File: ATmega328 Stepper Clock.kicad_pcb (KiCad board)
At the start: 2 copper layers, 80 x 80 mm, 9 parts, among them IC1 ATMEGA328-AU, J2 SBH11-PBPC-D05-ST-BK, Y1 Crystal

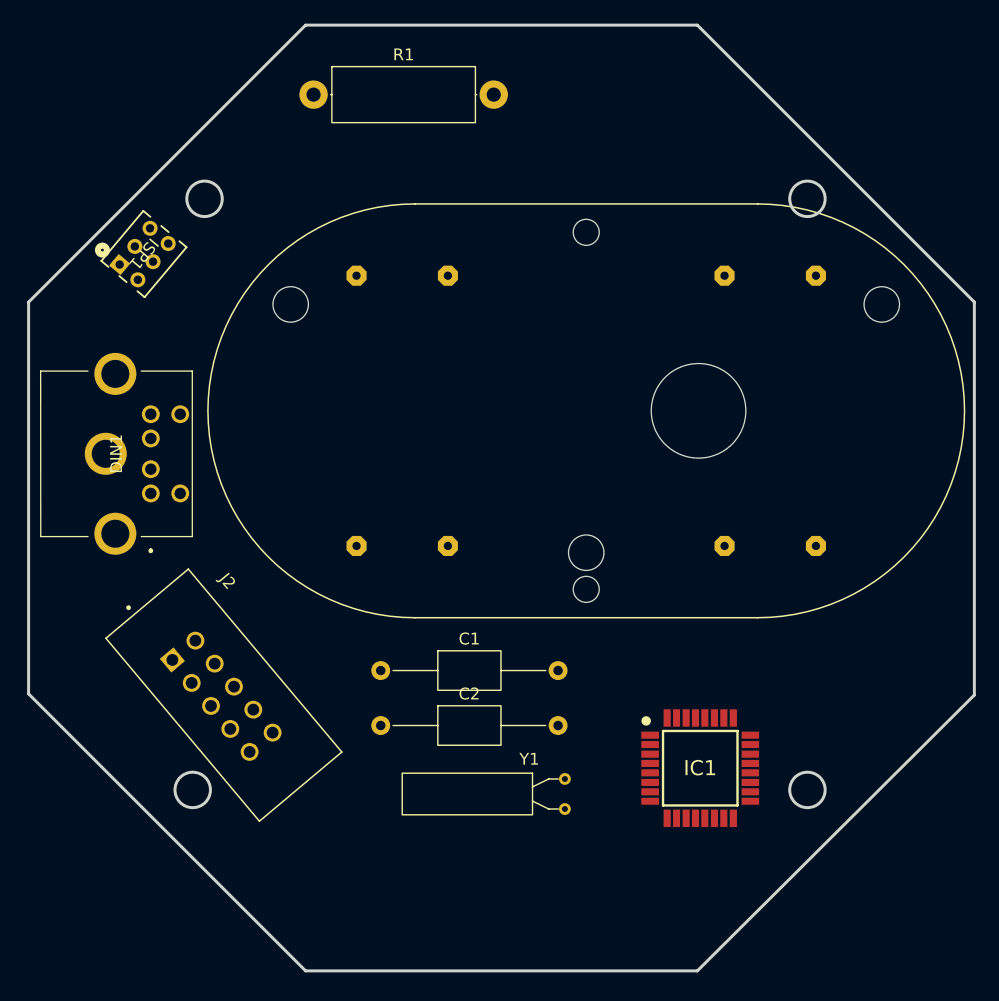
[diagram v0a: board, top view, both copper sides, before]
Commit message: Made a rough pcb layout , i made the frame using LibreCAD
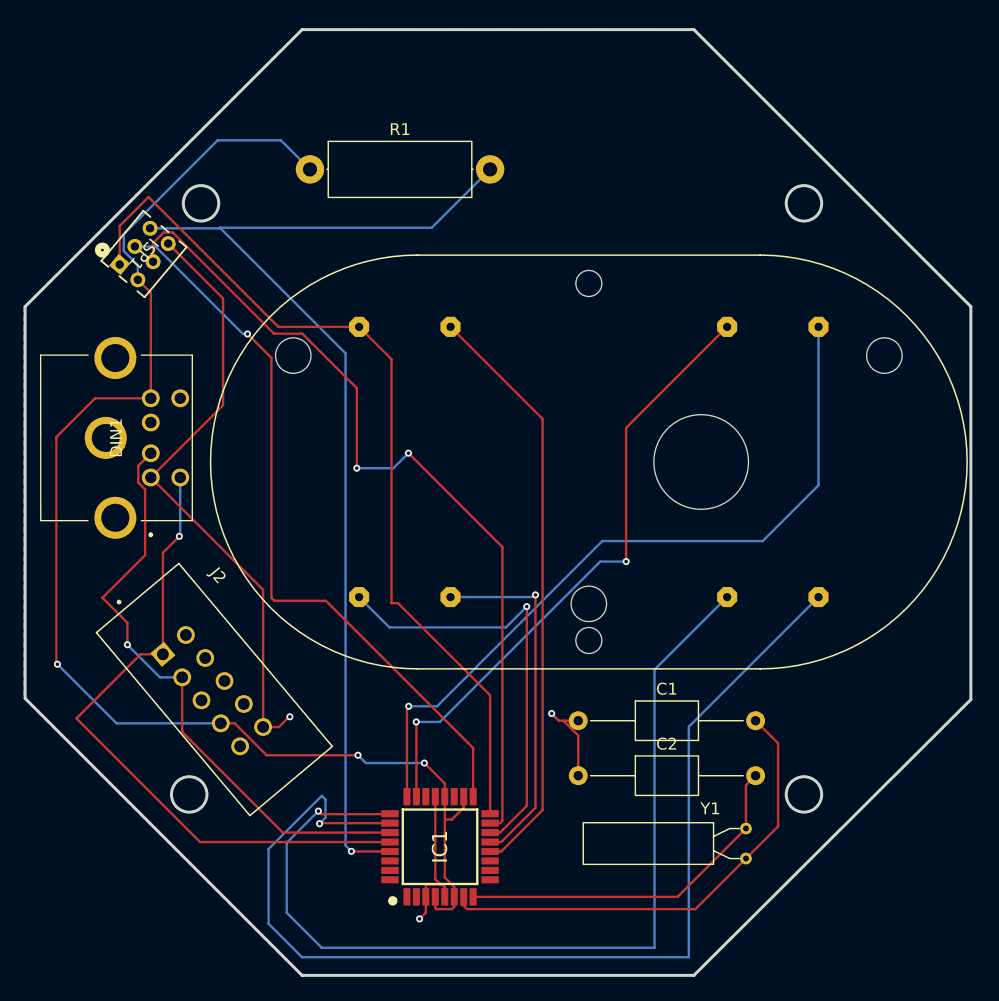
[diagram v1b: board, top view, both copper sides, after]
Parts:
- moved IC1 23.0 mm to (133.4, 121.4), turned to 90 degrees
- moved C1 17.2 mm to (145.0, 110.7)
- moved C2 17.2 mm to (145.0, 115.4)
- moved Y1 15.9 mm to (159.2, 119.9)
- moved R1 6.33 mm to (122.4, 64.1)
- moved VID28-1 4.33 mm to (145.9, 88.9)
- moved DIN1 1.35 mm to (108.9, 88.1)
- moved J2 0.93 mm to (114.2, 108.2)
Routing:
- net VCC: track 0.00 -> 116.7 mm, vias 0 -> 3
- net MOT_HOUR_C: track 0.00 -> 93.1 mm, vias 0 -> 1
- net RESET: track 0.00 -> 91.4 mm, vias 0 -> 1
- net MOT_HOUR_A: track 0.00 -> 80.4 mm, vias 0 -> 1
- net MISO&MOT_MINUTE_B: track 0.00 -> 75.2 mm
- net GND: track 0.00 -> 72.8 mm, vias 0 -> 3
- net MOSI: track 0.00 -> 71.8 mm, vias 0 -> 2
- net MOT_HOUR_D: track 0.00 -> 63.5 mm, vias 0 -> 1
- net SCK: track 0.00 -> 62.2 mm, vias 0 -> 1
- net SCL: track 0.00 -> 56.0 mm, vias 0 -> 1
- net MOT_HOUR_B: track 0.00 -> 53.1 mm, vias 0 -> 2
- net SDA: track 0.00 -> 50.7 mm, vias 0 -> 1
- net MOT_MINUTE_D: track 0.00 -> 50.0 mm
- net Net-(IC1-(PCINT6/XTAL1/TOSC1)_PB6): track 0.00 -> 40.1 mm
- net MOT_MINUTE_A: track 0.00 -> 36.9 mm, vias 0 -> 1
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- added copper zone on B.Cu, net GND

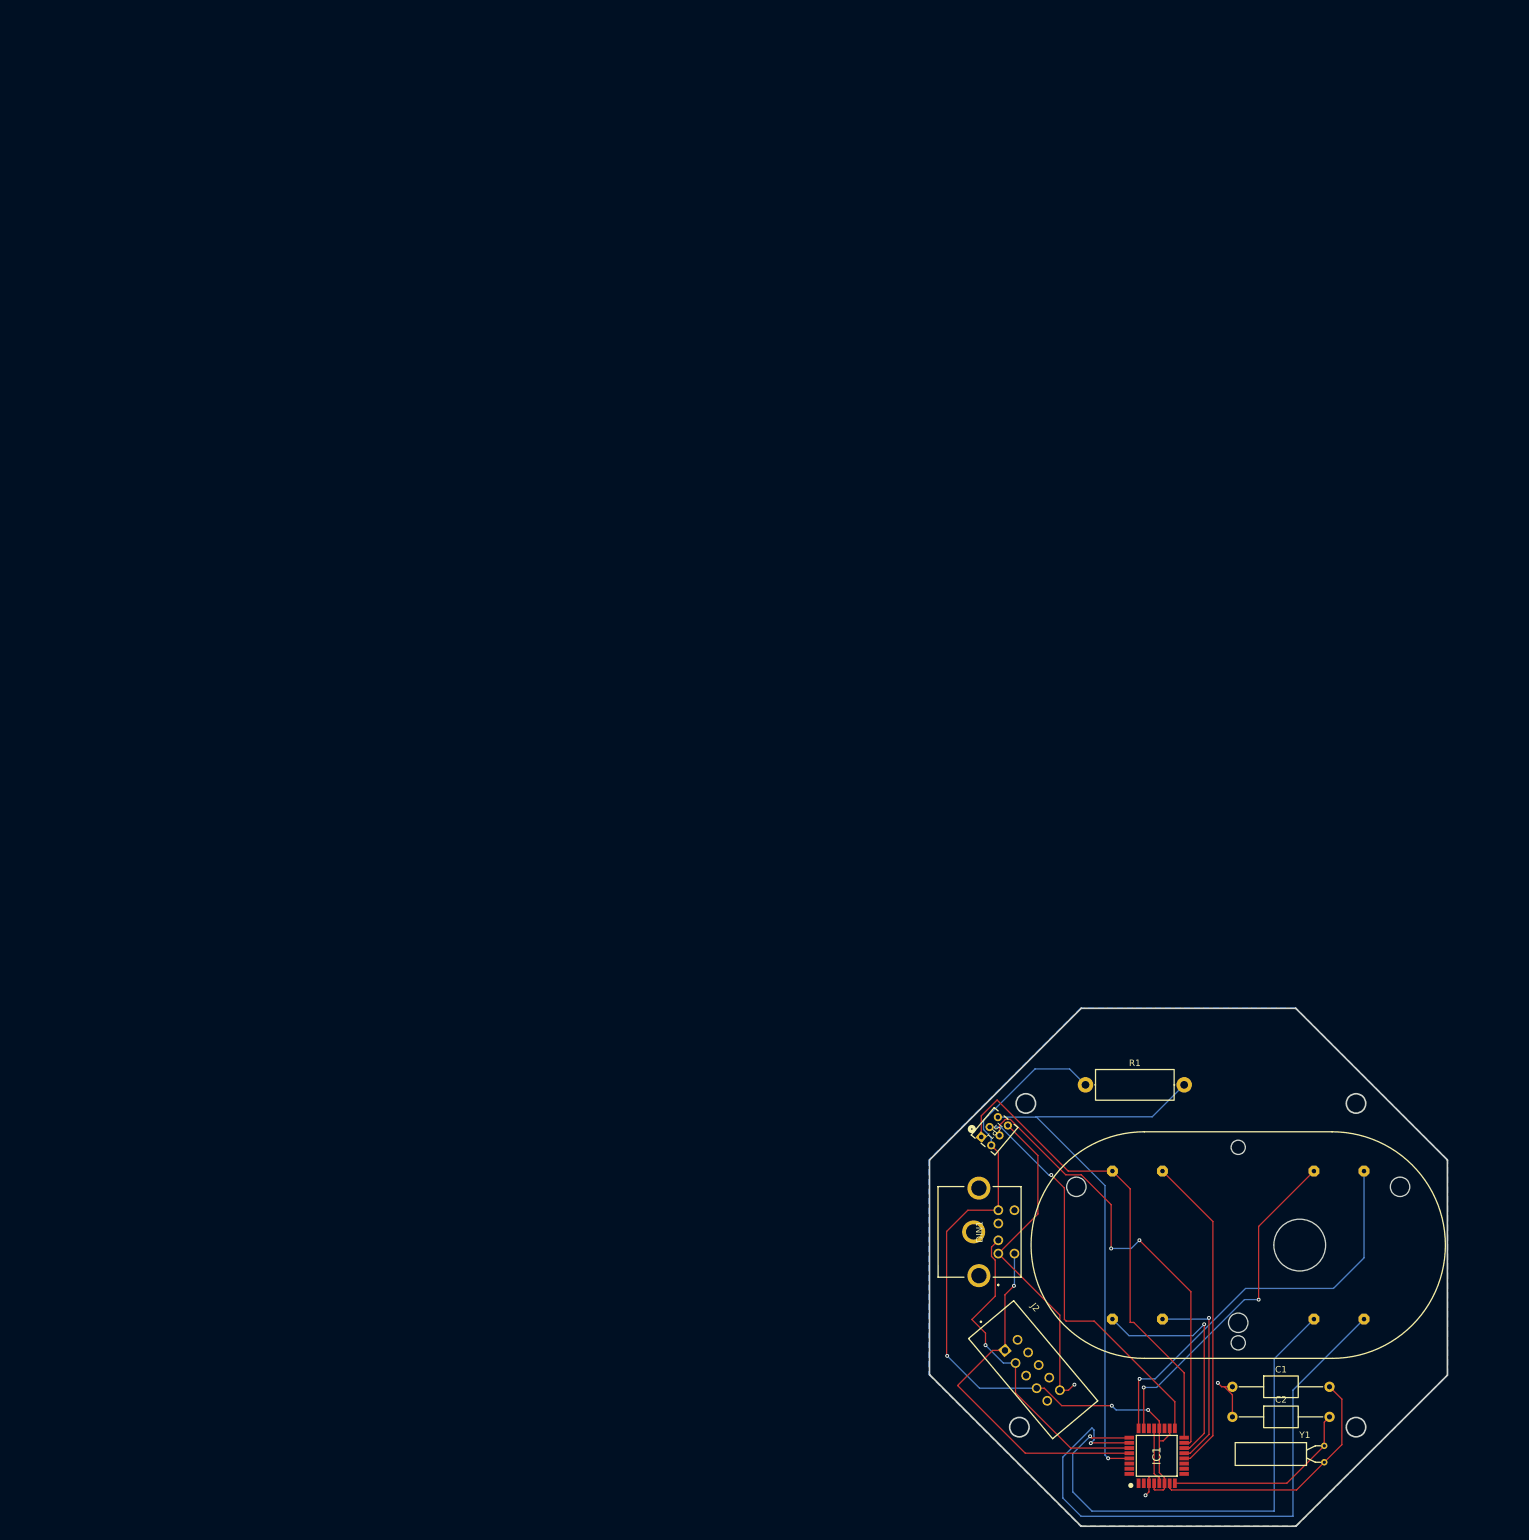
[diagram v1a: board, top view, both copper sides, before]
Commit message: Had to lot of changes like delete 10pin connectors,replace the DIN with 4-pin connector , hole size 3mm im starting the pcb layout all over again
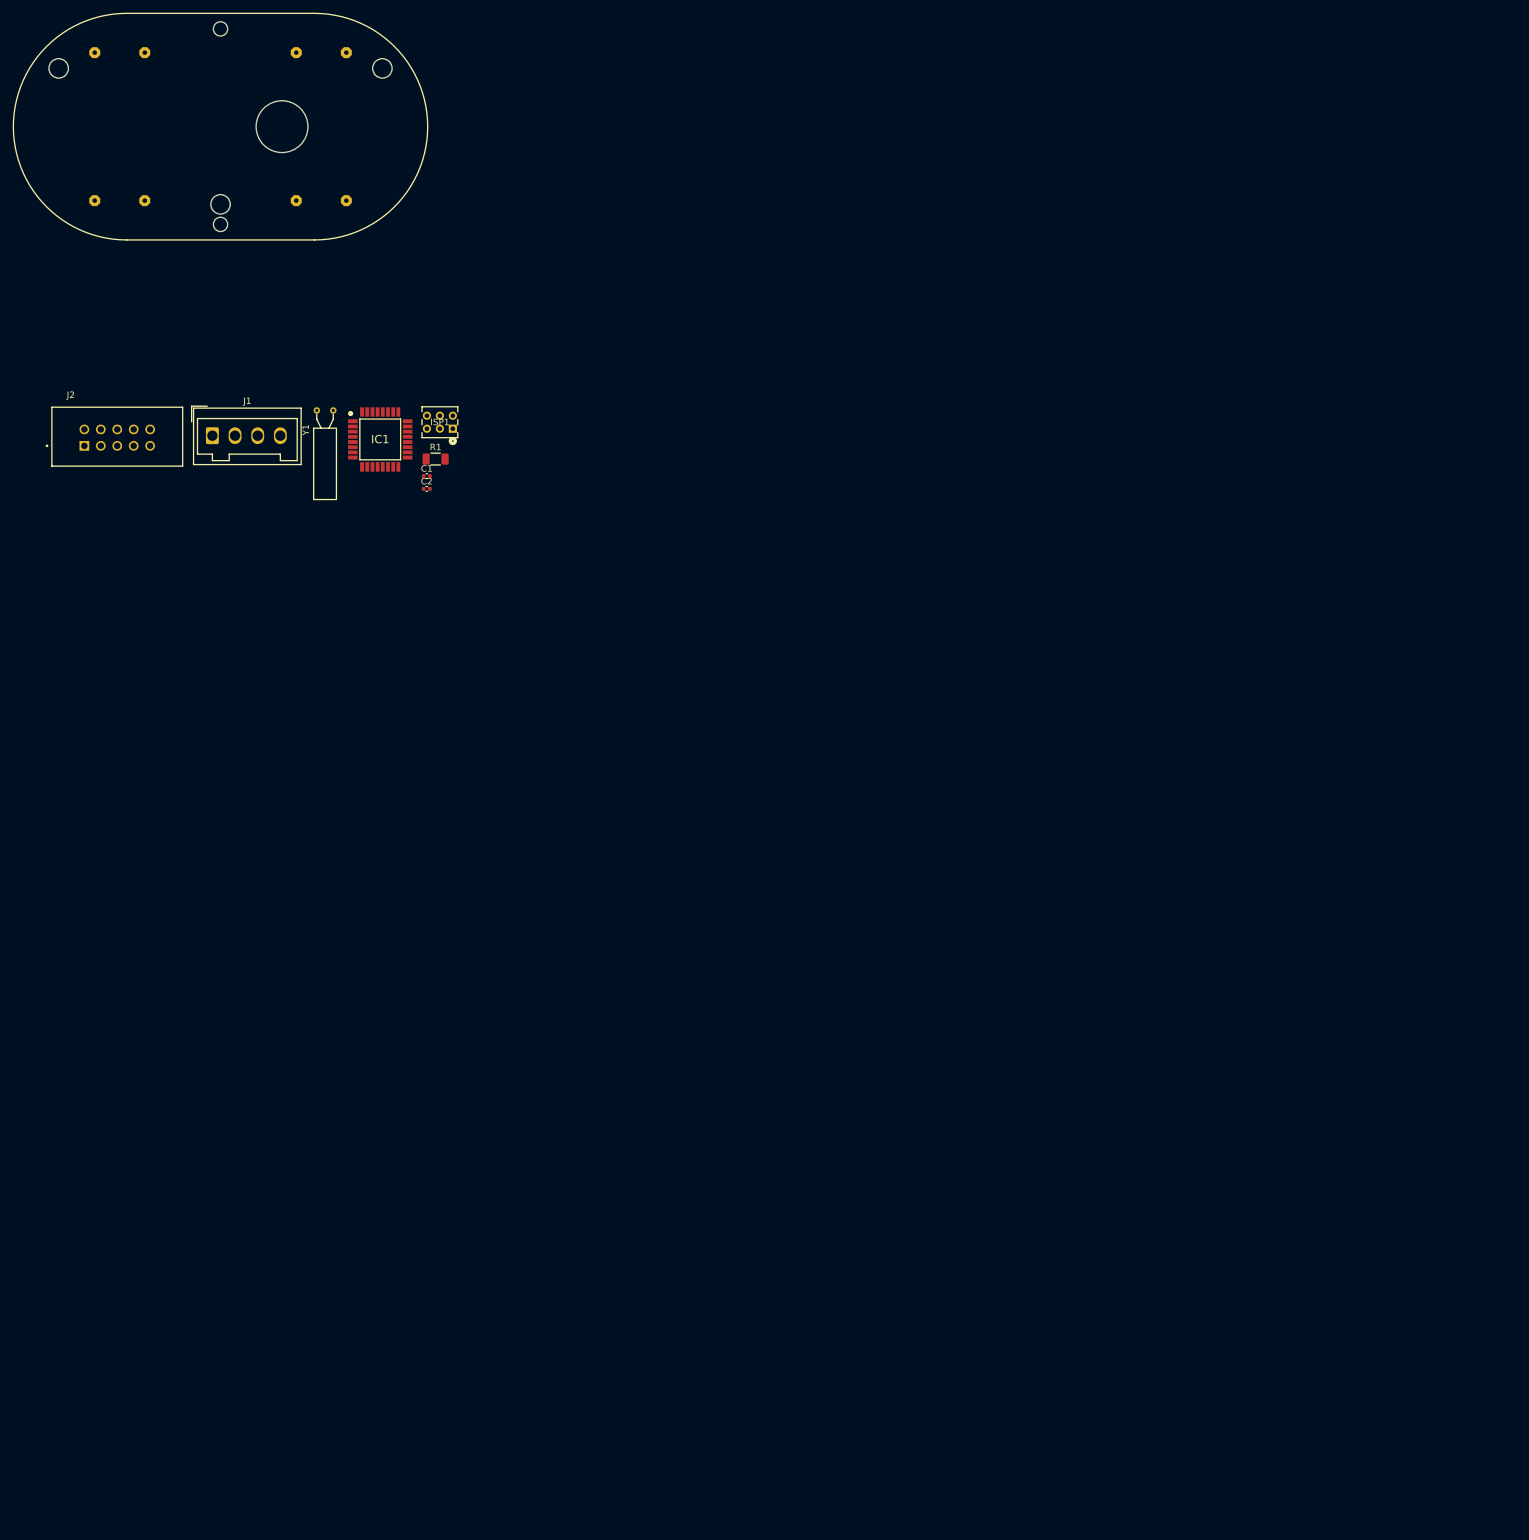
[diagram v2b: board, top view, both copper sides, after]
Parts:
- removed DIN1: 5750071-1, 5750071-1:57500711
- added J1: Conn_01x04_Pin, Connector_Wago:Wago_734-134_1x04_P3.50mm_Vertical, F.Cu at (-12.5, -36.2)
- C1, C2: footprint Capacitor_THT:C_Axial_L5.1mm_D3.1mm_P15.00mm_Horizontal -> Capacitor_SMD:C_0402_1005Metric
- R1: footprint Resistor_THT:R_Axial_DIN0414_L11.9mm_D4.5mm_P15.24mm_Horizontal -> Resistor_SMD:R_1206_3216Metric
- moved VID28-1 233.6 mm to (-11.3, -83.9)
- moved Y1 223.1 mm to (3.62, -40.1), turned to 0 degrees
- moved J2 201.8 mm to (-27.2, -35.9), turned to 0 degrees
- moved IC1 197.6 mm to (13.4, -35.6), turned to 0 degrees
- moved C2 189.8 mm to (20.6, -27.9)
- moved C1 187.8 mm to (20.6, -29.9)
- moved R1 139.4 mm to (22.0, -32.5)
- moved ISP1 139.0 mm to (22.6, -38.2), turned to 0 degrees
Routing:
- net VCC: track 116.7 -> 0.00 mm, vias 3 -> 0
- net MOT_HOUR_C: track 93.1 -> 0.00 mm, vias 1 -> 0
- net RESET: track 91.4 -> 0.00 mm, vias 1 -> 0
- net MOT_HOUR_A: track 80.4 -> 0.00 mm, vias 1 -> 0
- net MISO&MOT_MINUTE_B: track 75.2 -> 0.00 mm
- net GND: track 72.8 -> 0.00 mm, vias 3 -> 0
- net MOSI: track 71.8 -> 0.00 mm, vias 2 -> 0
- net MOT_HOUR_D: track 63.5 -> 0.00 mm, vias 1 -> 0
- net SCK: track 62.2 -> 0.00 mm, vias 1 -> 0
- net SCL: track 56.0 -> 0.00 mm, vias 1 -> 0
- net MOT_HOUR_B: track 53.1 -> 0.00 mm, vias 2 -> 0
- net SDA: track 50.7 -> 0.00 mm, vias 1 -> 0
- net MOT_MINUTE_D: track 50.0 -> 0.00 mm
- net Net-(IC1-(PCINT6/XTAL1/TOSC1)_PB6): track 40.1 -> 0.00 mm
- net MOT_MINUTE_A: track 36.9 -> 0.00 mm, vias 1 -> 0
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- removed copper zone on B.Cu, net GND
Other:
- board outline removed
